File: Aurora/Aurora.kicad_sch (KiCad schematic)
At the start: 2 parts, among them J1 UJ20-C-H-C-3-SMT-TR, U1 STM32H757BITx

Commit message: test
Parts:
- added C1: C, symbol Device:C
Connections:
- net at U1.7 (VDD): now also C1.1
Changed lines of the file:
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@@
+		)
+	)
+	(wire
+		(pts
+			(xy 166.37 71.12) (xy 166.37 91.44)
+		)
+		(stroke
+			(width 0)
+			(type default)
+		)
+	)
+	(wire
+		(pts
+			(xy 163.83 71.12) (xy 166.37 71.12)
+		)
+		(stroke
+			(width 0)
+			(type default)
 		)
 	)
@@
 	)
 	(symbol
+		(lib_id "power:+3.3V")
+		(at 138.43 87.63 0)
+		(unit 1)
+		(exclude_from_sim no)
+		(in_bom yes)
+		(on_board yes)
+		(dnp no)
+		(fields_autoplaced yes)
+		(property "Reference" "#PWR02"
+			(at 138.43 91.44 0)
+			(effects
+				(font
+					(size 1.27 1.27)
+				)
+				(hide yes)
+			)
+		)
+		(property "Value" "+3.3V"
+			(at 138.43 82.55 0)
+			(effects
+				(font
+					(size 1.27 1.27)
+				)
+			)
+		)
+		(property "Footprint" ""
+			(at 138.43 87.63 0)
+			(effects
+				(font
+					(size 1.27 1.27)
+				)
+				(hide yes)
+			)
+		)
+		(property "Datasheet" ""
+			(at 138.43 87.63 0)
+			(effects
+				(font
+					(size 1.27 1.27)
+				)
+				(hide yes)
+			)
+		)
+		(property "Description" "Power symbol creates a global label with name \"+3.3V\""
+			(at 138.43 87.63 0)
+			(effects
+				(font
+					(size 1.27 1.27)
+				)
+				(hide yes)
+			)
+		)
+		(pin "1"
+		)
+		(instances
+			(project ""
+				(path "/073f53a3-faa8-4419-bff2-f325850469a4"
+					(reference "#PWR02")
+					(unit 1)
+				)
+			)
+		)
+	)
+	(symbol
 		(lib_id "power:GND")
 		(at 194.31 332.74 0)
@@
 					(unit 1)
 				)
+			)
+		)
+	)
+	(symbol
+		(lib_id "Device:C")
+		(at 163.83 74.93 0)
+		(unit 1)
+		(exclude_from_sim no)
+		(in_bom yes)
+		(on_board yes)
+		(dnp no)
+		(fields_autoplaced yes)
+		(property "Reference" "C1"
+			(at 167.64 73.6599 0)
+			(effects
+				(font
+					(size 1.27 1.27)
+				)
+				(justify left)
+			)
+		)
+		(property "Value" "C"
+			(at 167.64 76.1999 0)
+			(effects
+				(font
+					(size 1.27 1.27)
+				)
+				(justify left)
+			)
+		)
+		(property "Footprint" ""
+			(at 164.7952 78.74 0)
+			(effects
+				(font
+					(size 1.27 1.27)
+				)
+				(hide yes)
+			)
+		)
+		(property "Datasheet" "~"
+			(at 163.83 74.93 0)
+			(effects
+				(font
+					(size 1.27 1.27)
+				)
+				(hide yes)
+			)
+		)
+		(property "Description" "Unpolarized capacitor"
+			(at 163.83 74.93 0)
+			(effects
+				(font
+					(size 1.27 1.27)
+				)
+				(hide yes)
+			)
+		)
+		(pin "1"
+		)
+		(pin "2"
+		)
+		(instances
+			(project ""
+				(path "/073f53a3-faa8-4419-bff2-f325850469a4"
+					(reference "C1")
+					(unit 1)
+				)

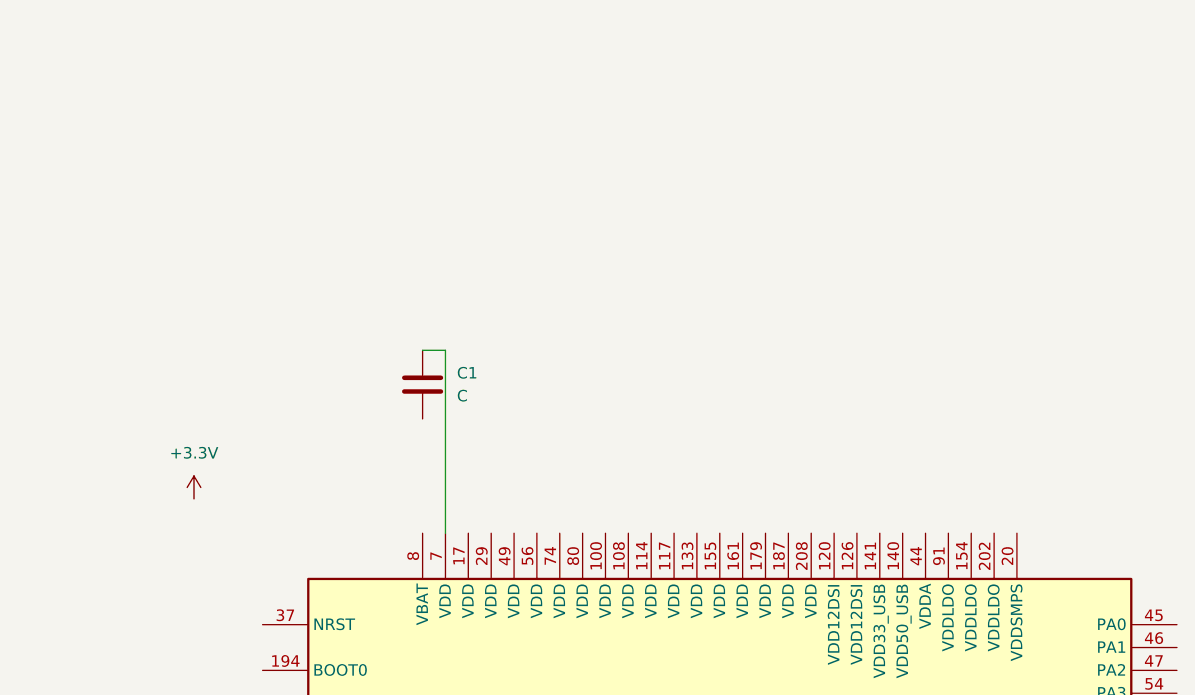
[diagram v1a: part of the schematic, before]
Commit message: hooked VDD pins to power, includes decoupling and bulk capacitors
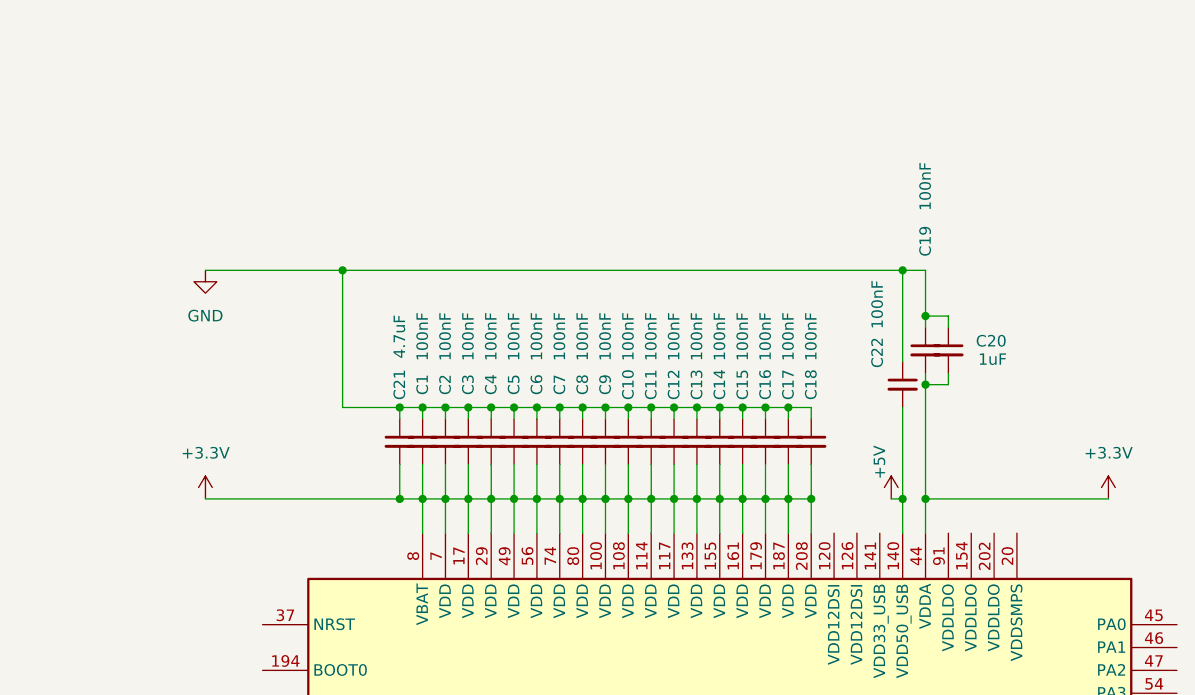
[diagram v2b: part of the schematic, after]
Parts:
- removed C1: C, symbol Device:C
- added C1, C10, C11, C12, C13, C14, C15, C16, C17, C18, C19, C2, C22, C3, C4, C5, C6, C7, C8, C9: 100nF, symbol Device:C_Small
- added C20: 1uF, symbol Device:C_Small
- added C21: 4.7uF, symbol Device:C_Small
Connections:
- net +3.3V: now also U1.100 (VDD), U1.108 (VDD), U1.114 (VDD), U1.117 (VDD), U1.133 (VDD), U1.155 (VDD), U1.161 (VDD), U1.17 (VDD), U1.179 (VDD), U1.187 (VDD), U1.208 (VDD), U1.29 (VDD), U1.44 (VDDA), U1.49 (VDD), U1.56 (VDD), U1.7 (VDD), U1.74 (VDD), U1.8 (VBAT), U1.80 (VDD), C1.2, C10.2, C11.2, C12.2, C13.2, C14.2, C15.2, C16.2, C17.2, C18.2, C19.2, C2.2, C20.2, C21.2, C3.2, C4.2, C5.2, C6.2, C7.2, C8.2, C9.2
- net GND: now also C1.1, C10.1, C11.1, C12.1, C13.1, C14.1, C15.1, C16.1, C17.1, C18.1, C19.1, C2.1, C20.1, C21.1, C22.1, C3.1, C4.1, C5.1, C6.1, C7.1, C8.1, C9.1
- net +5V: now reaches U1.140 (VDD50_USB)
- net +5V: now also C22.2

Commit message: finished power pins
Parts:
- added C23, C24: 100nF, symbol Device:C_Small
- added C25: 1uF, symbol Device:C_Small
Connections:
- net +3.3V: now also U1.141 (VDD33_USB)
- net +1.2V: now reaches U1.120 (VDD12DSI)
- net +1.2V: now also U1.126 (VDD12DSI), C23.2, C24.2, C25.2
- new net: C23.1, C24.1, C25.1

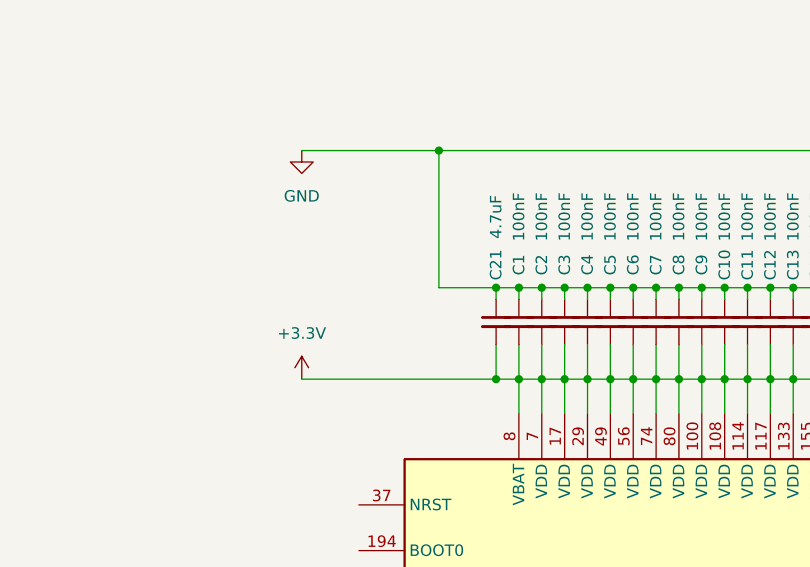
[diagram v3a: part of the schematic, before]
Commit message: fixed capacitors
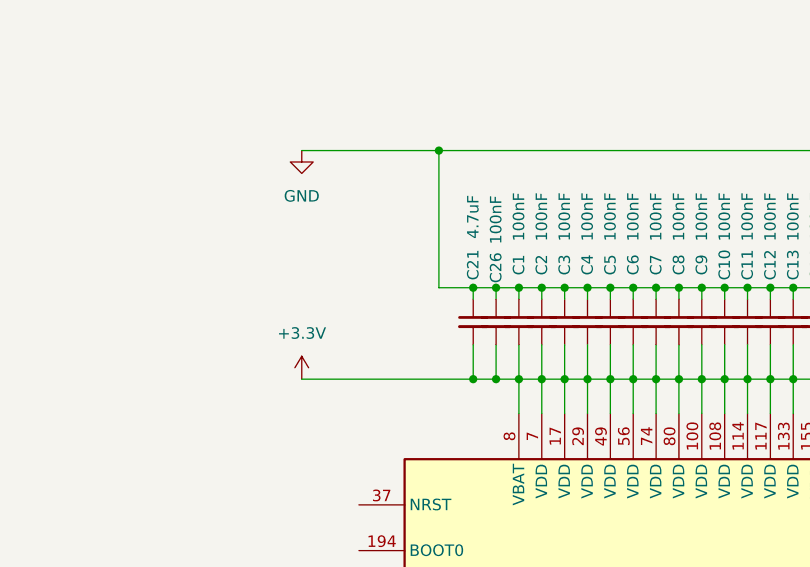
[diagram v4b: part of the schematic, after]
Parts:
- added C26: 100nF, symbol Device:C_Small
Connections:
- net +3.3V: now also C26.2
- net GND: now also C26.1
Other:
- moved on the sheet: C21
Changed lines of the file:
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@@
 	)
 	(junction
+		(at 158.75 87.63)
+		(diameter 0)
+		(color 0 0 0 0)
+	)
+	(junction
 		(at 163.83 87.63)
 		(diameter 0)
@@
 	)
 	(junction
+		(at 161.29 77.47)
+		(diameter 0)
+		(color 0 0 0 0)
+	)
+	(junction
 		(at 171.45 87.63)
 		(diameter 0)
@@
 	)
 	(junction
+		(at 158.75 77.47)
+		(diameter 0)
+		(color 0 0 0 0)
+	)
+	(junction
 		(at 212.09 90.17)
 		(diameter 0)
@@
 	)
 	(junction
-		(at 161.29 77.47)
-		(diameter 0)
-		(color 0 0 0 0)
-	)
-	(junction
-		(at 161.29 87.63)
-		(diameter 0)
-		(color 0 0 0 0)
-	)
-	(junction
 		(at 181.61 77.47)
 		(diameter 0)
@@
 	)
 	(junction
+		(at 161.29 87.63)
+		(diameter 0)
+		(color 0 0 0 0)
+	)
+	(junction
 		(at 154.94 62.23)
 		(diameter 0)
@@
 	(wire
 		(pts
-			(xy 161.29 87.63) (xy 163.83 87.63)
-		)
-		(stroke
-			(width 0)
-			(type default)
-		)
-	)
-	(wire
-		(pts
 			(xy 179.07 87.63) (xy 181.61 87.63)
 		)
@@
 	(wire
 		(pts
-			(xy 161.29 83.82) (xy 161.29 87.63)
+			(xy 158.75 83.82) (xy 158.75 87.63)
 		)
 		(stroke
@@
 	(wire
 		(pts
-			(xy 139.7 87.63) (xy 161.29 87.63)
+			(xy 139.7 87.63) (xy 158.75 87.63)
 		)
 		(stroke
@@
 	(wire
 		(pts
+			(xy 161.29 77.47) (xy 163.83 77.47)
+		)
+		(stroke
+			(width 0)
+			(type default)
+		)
+	)
+	(wire
+		(pts
 			(xy 208.28 91.44) (xy 208.28 90.17)
 		)
@@
 	(wire
 		(pts
-			(xy 154.94 77.47) (xy 161.29 77.47)
+			(xy 154.94 77.47) (xy 158.75 77.47)
 		)
 		(stroke
@@
 	(wire
 		(pts
-			(xy 161.29 77.47) (xy 161.29 78.74)
+			(xy 158.75 77.47) (xy 158.75 78.74)
 		)
 		(stroke
@@
 	(wire
 		(pts
-			(xy 184.15 77.47) (xy 184.15 78.74)
+			(xy 161.29 77.47) (xy 161.29 78.74)
 		)
 		(stroke
@@
 	(wire
 		(pts
-			(xy 204.47 87.63) (xy 207.01 87.63)
+			(xy 184.15 77.47) (xy 184.15 78.74)
 		)
 		(stroke
@@
 	(wire
 		(pts
-			(xy 173.99 77.47) (xy 176.53 77.47)
+			(xy 204.47 87.63) (xy 207.01 87.63)
 		)
 		(stroke
@@
 	(wire
 		(pts
-			(xy 161.29 77.47) (xy 163.83 77.47)
+			(xy 173.99 77.47) (xy 176.53 77.47)
 		)
 		(stroke
@@
 	(wire
 		(pts
+			(xy 158.75 87.63) (xy 161.29 87.63)
+		)
+		(stroke
+			(width 0)
+			(type default)
+		)
+	)
+	(wire
+		(pts
 			(xy 179.07 83.82) (xy 179.07 87.63)
 		)
@@
 	(wire
 		(pts
+			(xy 158.75 77.47) (xy 161.29 77.47)
+		)
+		(stroke
+			(width 0)
+			(type default)
+		)
+	)
+	(wire
+		(pts
 			(xy 194.31 87.63) (xy 194.31 91.44)
 		)
@@
 	(wire
 		(pts
+			(xy 161.29 83.82) (xy 161.29 87.63)
+		)
+		(stroke
+			(width 0)
+			(type default)
+		)
+	)
+	(wire
+		(pts
 			(xy 209.55 82.55) (xy 212.09 82.55)
 		)
@@
 	(wire
 		(pts
+			(xy 161.29 87.63) (xy 163.83 87.63)
+		)
+		(stroke
+			(width 0)
+			(type default)
+		)
+	)
+	(wire
+		(pts
 			(xy 219.71 74.93) (xy 219.71 73.66)
 		)
@@
 	)
 	(symbol
+		(lib_id "Device:C_Small")
+		(at 161.29 81.28 0)
+		(unit 1)
+		(exclude_from_sim no)
+		(in_bom yes)
+		(on_board yes)
+		(dnp no)
+		(property "Reference" "C26"
+			(at 161.29 76.962 90)
+			(effects
+				(font
+					(size 1.27 1.27)
+				)
+				(justify left)
+			)
+		)
+		(property "Value" "100nF"
+			(at 161.29 72.644 90)
+			(effects
+				(font
+					(size 1.27 1.27)
+				)
+				(justify left)
+			)
+		)
+		(property "Footprint" ""
+			(at 161.29 81.28 0)
+			(effects
+				(font
+					(size 1.27 1.27)
+				)
+				(hide yes)
+			)
+		)
+		(property "Datasheet" "~"
+			(at 161.29 81.28 0)
+			(effects
+				(font
+					(size 1.27 1.27)
+				)
+				(hide yes)
+			)
+		)
+		(property "Description" "Unpolarized capacitor, small symbol"
+			(at 161.29 81.28 0)
+			(effects
+				(font
+					(size 1.27 1.27)
+				)
+				(hide yes)
+			)
+		)
+		(pin "1"
+		)
+		(pin "2"
+		)
+		(instances
+			(project ""
+				(path "/073f53a3-faa8-4419-bff2-f325850469a4"
+					(reference "C26")
+					(unit 1)
+				)
+			)
+		)
+	)
+	(symbol
 		(lib_id "MCU_ST_STM32H7:STM32H757BITx")
 		(at 196.85 210.82 0)
@@
 	(symbol
 		(lib_id "Device:C_Small")
-		(at 161.29 81.28 0)
+		(at 158.75 81.28 0)
 		(unit 1)
 		(exclude_from_sim no)
@@
 		(dnp no)
 		(property "Reference" "C21"
-			(at 161.29 74.93 90)
+			(at 158.75 74.93 90)
 			(effects
 				(font
@@
 		)
 		(property "Value" "4.7uF"
-			(at 161.29 69.596 90)
+			(at 158.75 69.596 90)
 			(effects
 				(font
@@
 		)
 		(property "Footprint" ""
-			(at 161.29 81.28 0)
+			(at 158.75 81.28 0)
 			(effects
 				(font
@@
 		)
 		(property "Datasheet" "~"
-			(at 161.29 81.28 0)
+			(at 158.75 81.28 0)
 			(effects
 				(font
@@
 		)
 		(property "Description" "Unpolarized capacitor, small symbol"
-			(at 161.29 81.28 0)
+			(at 158.75 81.28 0)
 			(effects
 				(font
